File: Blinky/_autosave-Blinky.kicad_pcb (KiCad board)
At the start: 2 copper layers, 43.1 x 64.6 mm, 69 parts, among them J1 Conn_01x06_Socket, J2 Conn_01x06_Socket, J3 Battery Connector, J4 Charging Notches, Q1 IRLML6244, Q2 IRLML6244, Q3 IRLML6244, Q4 IRLML6244, Q5 IRLML6244, Q6 IRLML6244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

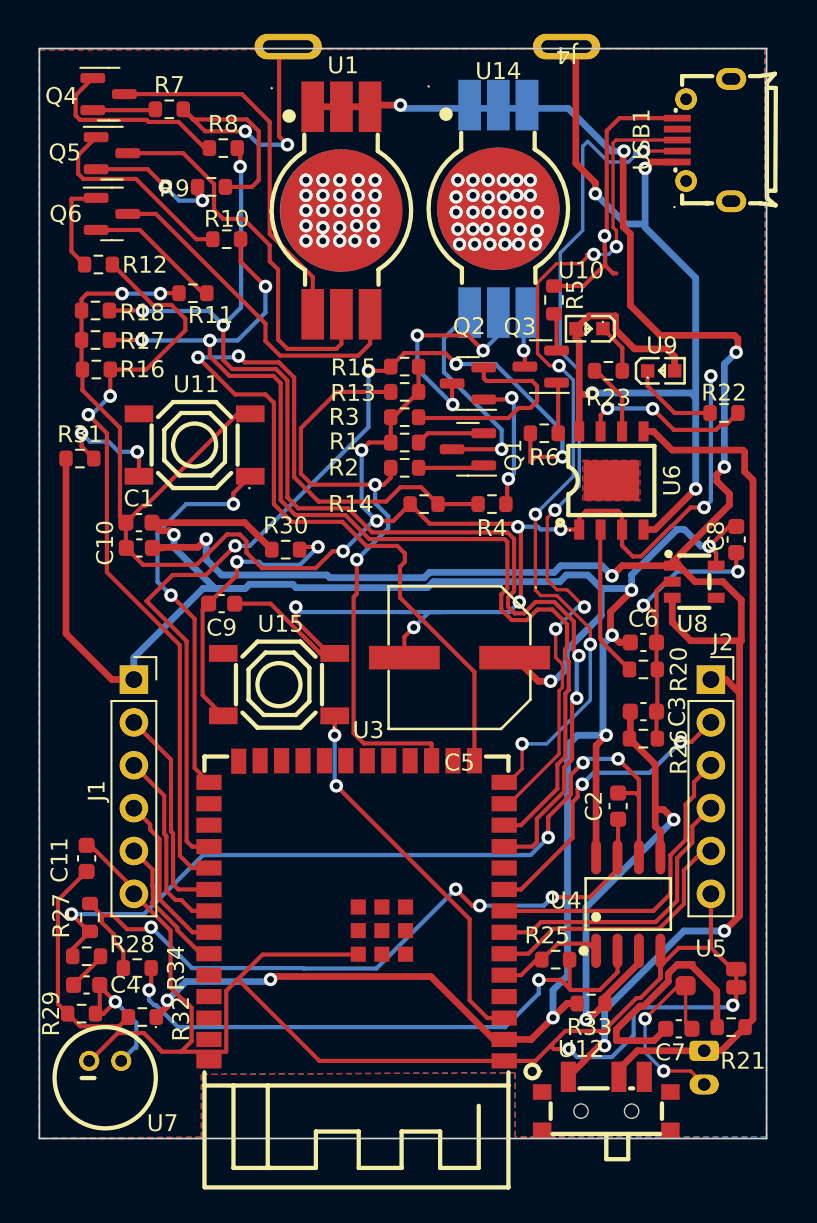
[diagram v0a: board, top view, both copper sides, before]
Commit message: 3d work and fixed 90 deg rotation in capacitor issue
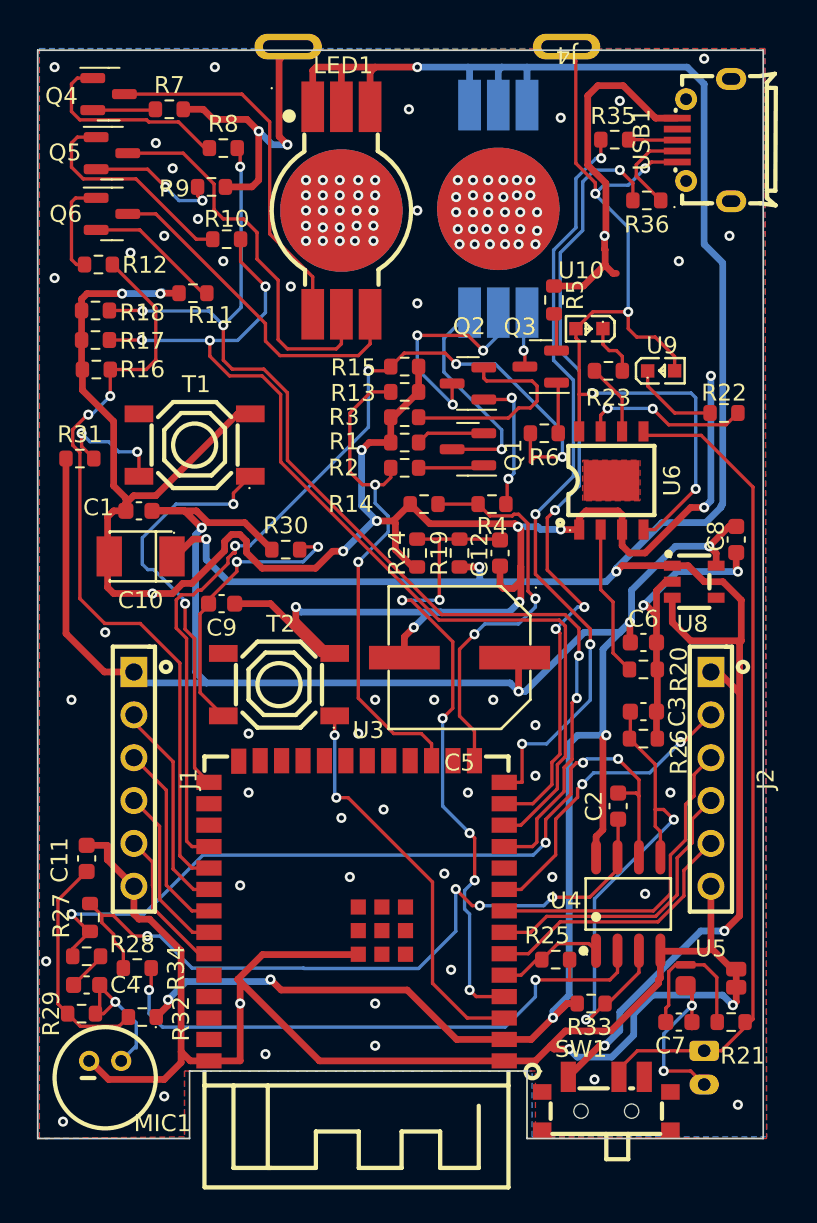
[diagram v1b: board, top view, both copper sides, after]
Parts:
- removed U13, U14: XL-HD6070RGBC-A46L, footprint:LED-SMD_XL-HD6070RGBC-A46L-BACKSIDE
- added C12: 100nF, Capacitor_SMD:C_0603_1608Metric, F.Cu at (152.4, 74.3)
- added R19: 470k, Resistor_SMD:R_0603_1608Metric, F.Cu at (150.0, 74.3)
- added R24: 470k, Resistor_SMD:R_0603_1608Metric, F.Cu at (147.5, 74.3)
- added R35: 10, Resistor_SMD:R_0603_1608Metric, F.Cu at (159.2, 49.8)
- added R36: 10, Resistor_SMD:R_0603_1608Metric, F.Cu at (161.1, 53.4)
- C10: footprint Capacitor_SMD:C_0603_1608Metric -> footprint:CASE-B_3528
- J1, J2: footprint Connector_PinSocket_2.54mm:PinSocket_1x06_P2.54mm_Vertical -> footprint:HDR-TH_6P-P2.54-V-F
- LED1: renamed from U1; footprint footprint:LED-SMD_XL-HD6070RGBC-A46L -> Library:LED-SMD_XL-HD6070RGBC-A46L
- LED2: renamed from U2; footprint footprint:LED-SMD_XL-HD6070RGBC-A46L -> Library:LED-SMD_XL-HD6070RGBC-A46L
- moved J1 5.90 mm to (130.7, 87.7), turned to -90 degrees
- moved J2 5.90 mm to (164.9, 87.7), turned to -90 degrees
- moved C1 0.70 mm to (131.0, 71.8)
- moved C10 0.51 mm to (131.1, 74.5), turned to 180 degrees
- moved C7 0.40 mm to (163.0, 102.1)
- moved R21 0.30 mm to (166.1, 102.1)
- renumbered U7 to MIC1, U12 to SW1, U11 to T1, U15 to T2
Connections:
- C10 pad 1: GND -> VBAT
- C10 pad 2: VBAT -> GND
- U3 pad 4: unconnected-(U3-IO4-Pad4) -> /VBAT_MESS
- USB1 pad 2: /USB- -> Net-(USB1-D-)
- USB1 pad 3: /USB+ -> Net-(USB1-D+)
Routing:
- net /VBAT_MESS: track 0.00 -> 39.2 mm, vias 0 -> 6
- net /GREEN2: track 59.3 -> 23.6 mm
- net VBAT: track 132.4 -> 151.6 mm, vias 8 -> 6
- net GND: track 279.1 -> 291.8 mm, vias 19 -> 67
- net CHARGE+: track 61.2 -> 54.2 mm, vias 4 -> 5
- net /RED2: track 37.0 -> 30.1 mm
- net /USB+: track 52.5 -> 45.8 mm, vias 6 -> 4
- net Net-(USB1-D-): track 0.00 -> 5.48 mm
- net /GREEN1: track 65.2 -> 59.8 mm
- net /BLUE1: track 71.2 -> 66.0 mm
- net VDD: track 150.8 -> 146.1 mm, vias 9 -> 8
- net Net-(U5-VDD): track 14.5 -> 9.86 mm
- net /USB-: track 51.4 -> 47.6 mm
- net Net-(USB1-D+): track 0.00 -> 2.94 mm
- net /BLUE2: track 56.5 -> 54.5 mm
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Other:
- board size 43.1 x 64.6 mm -> 43 x 64.5 mm
